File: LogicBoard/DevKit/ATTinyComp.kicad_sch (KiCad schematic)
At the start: 11 parts, among them J21 UARTDBG, U16 ATTINY1616-MNR, U2 TPL0401B-10DCKR

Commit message: cleanup
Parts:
- C53, C55: footprint Capacitor_SMD:C_0402_1005Metric -> GigaVescLibs:C_0603_1608Metric_L; MPN C52923 -> C15849
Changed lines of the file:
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@@
       (effects (font (size 1.27 1.27)) (justify left))
     )
-    (property "Footprint" "Capacitor_SMD:C_0402_1005Metric" (at 93.6752 104.14 0)
+    (property "Footprint" "GigaVescLibs:C_0603_1608Metric_L" (at 93.6752 104.14 0)
       (effects (font (size 1.27 1.27)) hide)
     )
@@
       (effects (font (size 1.27 1.27)) hide)
     )
-    (property "MPN" "C52923" (at 92.71 100.33 0)
+    (property "MPN" "C15849" (at 92.71 100.33 0)
       (effects (font (size 1.27 1.27)) hide)
     )
@@
       (effects (font (size 1.27 1.27)) (justify left))
     )
-    (property "Footprint" "Capacitor_SMD:C_0402_1005Metric" (at 136.8552 60.96 0)
+    (property "Footprint" "GigaVescLibs:C_0603_1608Metric_L" (at 136.8552 60.96 0)
       (effects (font (size 1.27 1.27)) hide)
     )
@@
       (effects (font (size 1.27 1.27)) hide)
     )
-    (property "MPN" "C52923" (at 135.89 57.15 0)
+    (property "MPN" "C15849" (at 135.89 57.15 0)
       (effects (font (size 1.27 1.27)) hide)
     )

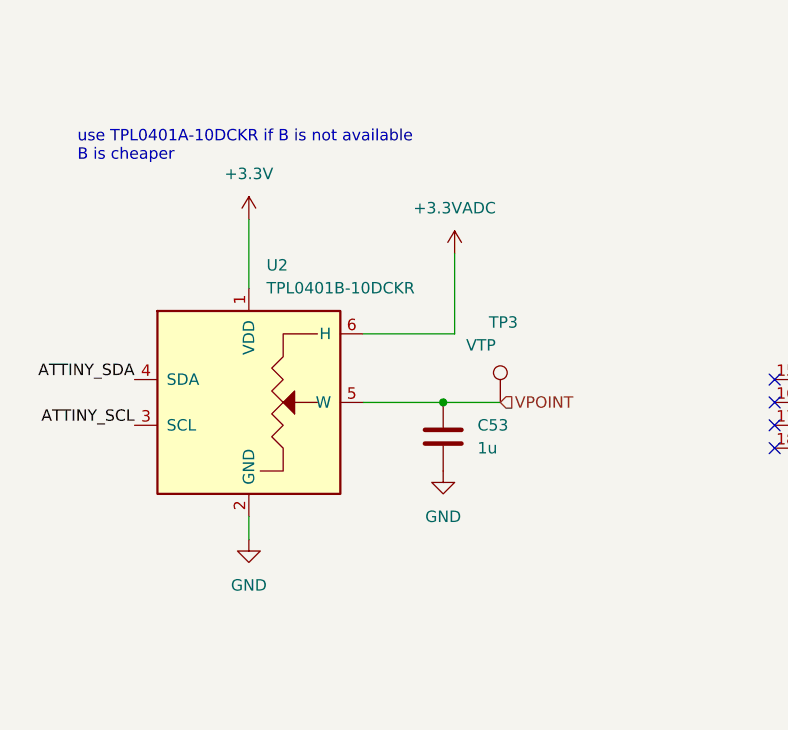
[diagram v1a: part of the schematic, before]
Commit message: v2.4 - INA4181A1IPWR
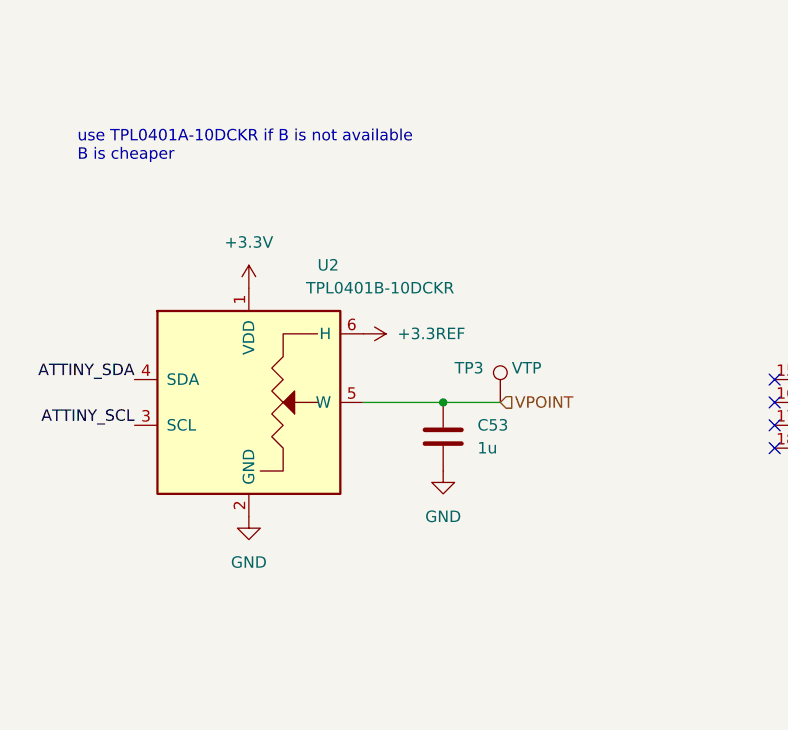
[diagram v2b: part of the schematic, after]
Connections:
- net +3.3VADC renamed +3.3REF
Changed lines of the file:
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@@
   (no_connect (at 129.54 96.52))
   (no_connect (at 129.54 99.06))
-  (wire (pts (xy 71.12 76.2) (xy 71.12 83.82))
-    (stroke (width 0) (type default))
-  )
   (wire (pts (xy 144.78 53.34) (xy 144.78 66.04))
     (stroke (width 0) (type default))
   )
-  (wire (pts (xy 71.12 109.22) (xy 71.12 111.76))
-    (stroke (width 0) (type default))
-  )
   (wire (pts (xy 135.89 53.34) (xy 144.78 53.34))
     (stroke (width 0) (type default))
   )
-  (wire (pts (xy 93.98 80.01) (xy 93.98 88.9))
-    (stroke (width 0) (type default))
-  )
   (wire (pts (xy 160.02 71.12) (xy 166.37 71.12))
     (stroke (width 0) (type default))
@@
   )
   (wire (pts (xy 92.71 96.52) (xy 99.06 96.52))
-    (stroke (width 0) (type default))
-  )
-  (wire (pts (xy 93.98 88.9) (xy 83.82 88.9))
     (stroke (width 0) (type default))
   )
@@
     )
   )
-  (symbol (lib_id "power:+3.3V") (at 71.12 76.2 0) (unit 1)
-    (in_bom yes) (on_board yes) (dnp no) (fields_autoplaced)
-    (property "Reference" "#PWR085" (at 71.12 80.01 0)
-      (effects (font (size 1.27 1.27)) hide)
-    )
-    (property "Value" "+3.3V" (at 71.12 71.12 0)
-      (effects (font (size 1.27 1.27)))
-    )
-    (property "Footprint" "" (at 71.12 76.2 0)
-      (effects (font (size 1.27 1.27)) hide)
-    )
-    (property "Datasheet" "" (at 71.12 76.2 0)
+  (symbol (lib_id "power:+3.3V") (at 71.12 83.82 0) (unit 1)
+    (in_bom yes) (on_board yes) (dnp no) (fields_autoplaced)
+    (property "Reference" "#PWR085" (at 71.12 87.63 0)
+      (effects (font (size 1.27 1.27)) hide)
+    )
+    (property "Value" "+3.3V" (at 71.12 78.74 0)
+      (effects (font (size 1.27 1.27)))
+    )
+    (property "Footprint" "" (at 71.12 83.82 0)
+      (effects (font (size 1.27 1.27)) hide)
+    )
+    (property "Datasheet" "" (at 71.12 83.82 0)
       (effects (font (size 1.27 1.27)) hide)
     )
@@
     )
   )
-  (symbol (lib_id "power:+3.3VADC") (at 93.98 80.01 0) (unit 1)
-    (in_bom yes) (on_board yes) (dnp no) (fields_autoplaced)
-    (property "Reference" "#PWR0127" (at 97.79 81.28 0)
-      (effects (font (size 1.27 1.27)) hide)
-    )
-    (property "Value" "+3.3VADC" (at 93.98 74.93 0)
-      (effects (font (size 1.27 1.27)))
-    )
-    (property "Footprint" "" (at 93.98 80.01 0)
-      (effects (font (size 1.27 1.27)) hide)
-    )
-    (property "Datasheet" "" (at 93.98 80.01 0)
-      (effects (font (size 1.27 1.27)) hide)
-    )
-    (pin "1")
-    (instances
-      (project "DevKit"
-        (path "/768a484b-8a27-40cf-8cad-0f63935b1af0/81081265-f675-4f9d-bffe-8ec1eaaaba23"
-          (reference "#PWR0127") (unit 1)
-        )
-        (path "/768a484b-8a27-40cf-8cad-0f63935b1af0/81081265-f675-4f9d-bffe-8ec1eaaaba23/4e84f19f-3250-45a9-9b88-20e811e150a6"
-          (reference "#PWR085") (unit 1)
-        )
-        (path "/768a484b-8a27-40cf-8cad-0f63935b1af0/81081265-f675-4f9d-bffe-8ec1eaaaba23/ac734765-aa76-45cd-b5a0-b23ad6c1564a"
-          (reference "#PWR0129") (unit 1)
-        )
-      )
-      (project "HardwareProtection"
-        (path "/a0bc7e80-607b-4b14-b86e-d486e2d36eac"
-          (reference "#PWR014") (unit 1)
-        )
-      )
-    )
-  )
   (symbol (lib_id "Potentiometer_Digital:TPL0401B-10-Q1") (at 71.12 96.52 0) (unit 1)
-    (in_bom yes) (on_board yes) (dnp no) (fields_autoplaced)
-    (property "Reference" "U2" (at 73.0759 81.28 0)
+    (in_bom yes) (on_board yes) (dnp no)
+    (property "Reference" "U2" (at 78.74 81.28 0)
       (effects (font (size 1.27 1.27)) (justify left))
     )
-    (property "Value" "TPL0401B-10DCKR" (at 73.0759 83.82 0)
+    (property "Value" "TPL0401B-10DCKR" (at 77.47 83.82 0)
       (effects (font (size 1.27 1.27)) (justify left))
     )
@@
   (symbol (lib_id "Connector:TestPoint") (at 99.06 96.52 0) (unit 1)
     (in_bom yes) (on_board yes) (dnp no)
-    (property "Reference" "TP3" (at 97.79 87.63 0)
+    (property "Reference" "TP3" (at 93.98 92.71 0)
       (effects (font (size 1.27 1.27)) (justify left))
     )
-    (property "Value" "VTP" (at 95.25 90.17 0)
+    (property "Value" "VTP" (at 100.33 92.71 0)
       (effects (font (size 1.27 1.27)) (justify left))
     )
@@
     )
   )
-  (symbol (lib_id "power:GND") (at 71.12 111.76 0) (unit 1)
-    (in_bom yes) (on_board yes) (dnp no) (fields_autoplaced)
-    (property "Reference" "#PWR088" (at 71.12 118.11 0)
-      (effects (font (size 1.27 1.27)) hide)
-    )
-    (property "Value" "GND" (at 71.12 116.84 0)
-      (effects (font (size 1.27 1.27)))
-    )
-    (property "Footprint" "" (at 71.12 111.76 0)
-      (effects (font (size 1.27 1.27)) hide)
-    )
-    (property "Datasheet" "" (at 71.12 111.76 0)
-      (effects (font (size 1.27 1.27)) hide)
-    )
+  (symbol (lib_id "GigaVescSymbols:+3.3REF") (at 83.82 88.9 270) (unit 1)
+    (in_bom yes) (on_board yes) (dnp no) (fields_autoplaced)
+    (property "Reference" "#PWR017" (at 80.01 88.9 0)
+      (effects (font (size 1.27 1.27)) hide)
+    )
+    (property "Value" "+3.3REF" (at 87.63 88.9 90)
+      (effects (font (size 1.27 1.27)) (justify left))
+    )
+    (property "Footprint" "" (at 83.82 88.9 0)
+      (effects (font (size 1.27 1.27)) hide)
+    )
+    (property "Datasheet" "" (at 83.82 88.9 0)
+      (effects (font (size 1.27 1.27)) hide)
+    )
+    (pin "1")
+    (instances
+      (project "DevKit"
+        (path "/768a484b-8a27-40cf-8cad-0f63935b1af0/717cb4b7-b47a-435c-946f-7c938a1d7e5f"
+          (reference "#PWR017") (unit 1)
+        )
+        (path "/768a484b-8a27-40cf-8cad-0f63935b1af0/81081265-f675-4f9d-bffe-8ec1eaaaba23/ac734765-aa76-45cd-b5a0-b23ad6c1564a"
+          (reference "#PWR017") (unit 1)
+        )
+        (path "/768a484b-8a27-40cf-8cad-0f63935b1af0/81081265-f675-4f9d-bffe-8ec1eaaaba23/4e84f19f-3250-45a9-9b88-20e811e150a6"
+          (reference "#PWR0203") (unit 1)
+        )
+      )
+    )
+  )
+  (symbol (lib_id "power:GND") (at 71.12 109.22 0) (unit 1)
+    (in_bom yes) (on_board yes) (dnp no) (fields_autoplaced)
+    (property "Reference" "#PWR088" (at 71.12 115.57 0)
+      (effects (font (size 1.27 1.27)) hide)
+    )
+    (property "Value" "GND" (at 71.12 114.3 0)
+      (effects (font (size 1.27 1.27)))
+    )
+    (property "Footprint" "" (at 71.12 109.22 0)
+      (effects (font (size 1.27 1.27)) hide)
+    )
+    (property "Datasheet" "" (at 71.12 109.22 0)
+      (effects (font (size 1.27 1.27)) hide)
+    )

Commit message: v3.2.0 - Moving to kicad 8
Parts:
- renumbered D9 to D10, R1 to R20, R1 to R43, R47 to R44, U2 to U1, U16 to U2

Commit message: v3.2.2 - TL494V2
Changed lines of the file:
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@@
 			)
 		)
-		(property "Description" ""
+		(property "Description" "Power symbol creates a global label with name \"GND\" , ground"
 			(at 144.78 111.76 0)
 			(effects
@@
 			)
 		)
-		(property "Description" ""
+		(property "Description" "Power symbol creates a global label with name \"+3.3V\""
 			(at 71.12 83.82 0)
 			(effects
@@
 			)
 		)
-		(property "Description" ""
+		(property "Description" "Power symbol creates a global label with name \"GND\" , ground"
 			(at 92.71 104.14 0)
 			(effects
@@
 			)
 		)
-		(property "Description" ""
+		(property "Description" "Power symbol creates a global label with name \"+3.3V\""
 			(at 72.39 46.99 0)
 			(effects
@@
 			)
 		)
-		(property "Description" ""
+		(property "Description" "Power symbol creates a global label with name \"+3.3V\""
 			(at 144.78 49.53 0)
 			(effects
@@
 			)
 		)
-		(property "Description" ""
+		(property "Description" "Power symbol creates a global label with name \"GND\" , ground"
 			(at 135.89 60.96 0)
 			(effects
@@
 			)
 		)
-		(property "Description" ""
+		(property "Description" "Power symbol creates a global label with name \"+3.3V\""
 			(at 72.39 40.64 0)
 			(effects
@@
 			)
 		)
-		(property "Description" ""
+		(property "Description" "Power symbol creates a global label with name \"GND\" , ground"
 			(at 71.12 109.22 0)
 			(effects
@@
 		)
 		(property "Value" "GND"
-			(at 160.02 30.48 90)
+			(at 160.02 30.4799 90)
 			(effects
 				(font
@@
 			)
 		)
-		(property "Description" ""
+		(property "Description" "Power symbol creates a global label with name \"GND\" , ground"
 			(at 156.21 30.48 0)
 			(effects

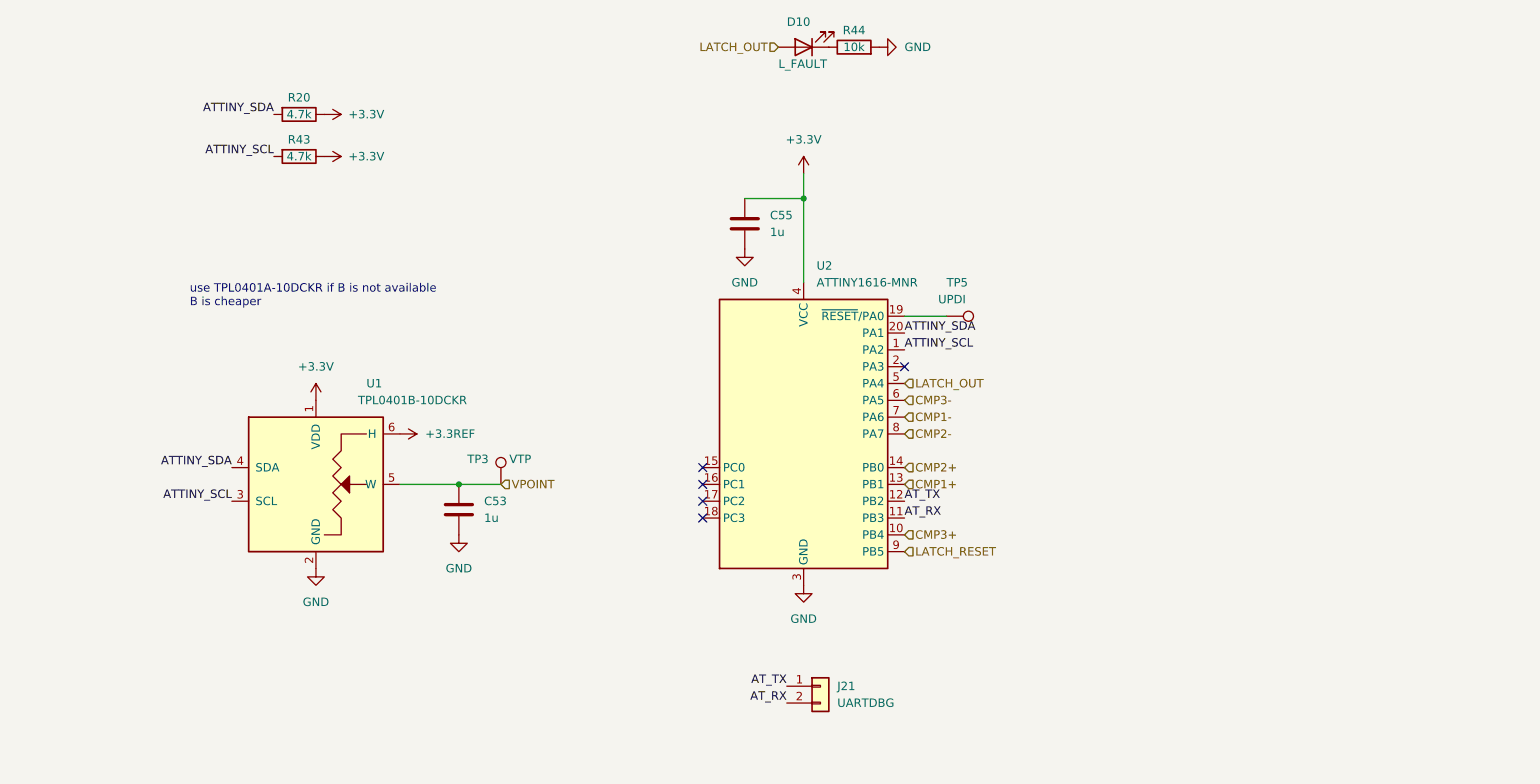
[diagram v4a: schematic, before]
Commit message: v3.3.2 - ECP2304 changes
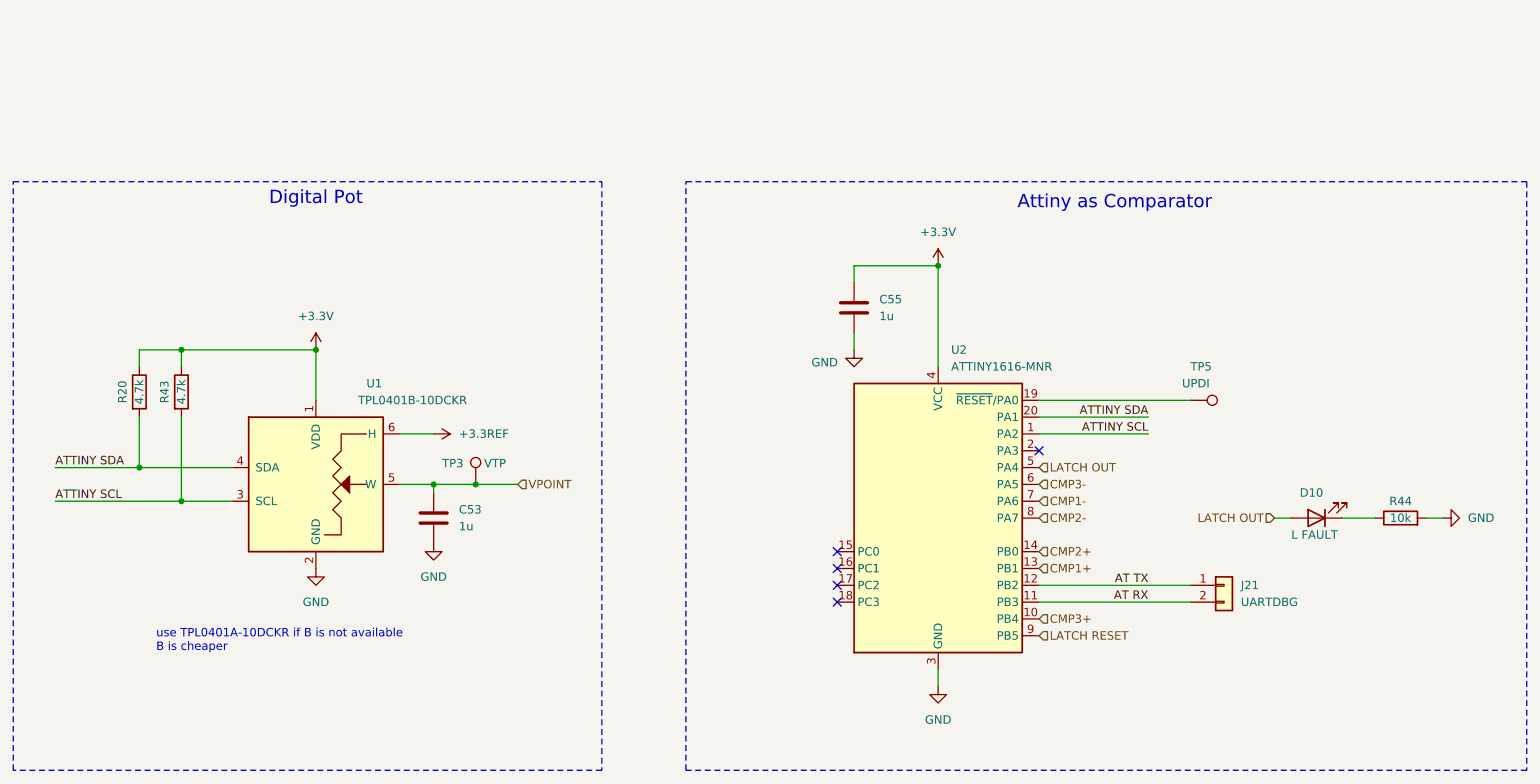
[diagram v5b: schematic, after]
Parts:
- D10: value L_FAULT -> L FAULT
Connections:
- net ATTINY_SCL renamed ATTINY SCL
- net ATTINY_SDA renamed ATTINY SDA
- net AT_RX renamed AT RX
- net AT_TX renamed AT TX
- net LATCH_OUT renamed LATCH OUT
- net LATCH_RESET renamed LATCH RESET
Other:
- note added: "Attiny as Comparator"
- note added: "Digital Pot"
- moved on the sheet: C53, C55, D10, J21, R20, R43, R44, TP3, TP5, U2
